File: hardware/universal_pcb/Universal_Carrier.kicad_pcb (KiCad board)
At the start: 2 copper layers, 100 x 85 mm, 24 parts, among them J1 ESP32_T_LANDSCAPE, J10 RACK_CREMALHEIRA, J11 PWR_ESP_5V, J12 PWR_SERVO_5V, J2 ESP32_B_LANDSCAPE, J3 SX1278_LORA_2x4, J4 BATT_APM, J5 BUZZER, J6 GPS_LC29H_7PIN, J7 ESC_PROP_UP, J8 RUDDER_DN, J9 WINCH_MODE, SW1 UP, SW2 MODE, SW3 DOWN, SW4 BOOT

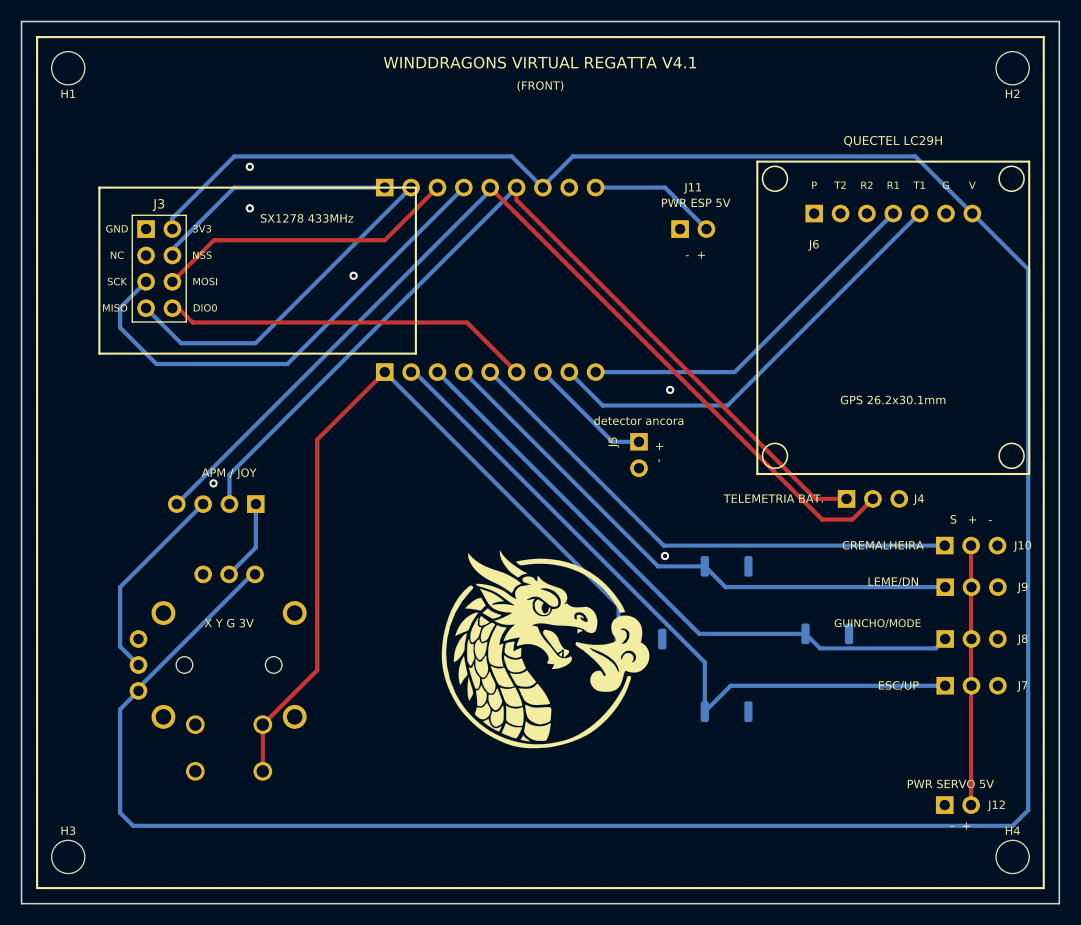
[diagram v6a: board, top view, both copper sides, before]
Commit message: feat: add ESP32-C6-LCD-1.47 hardware models and update Universal Carrier PCB design
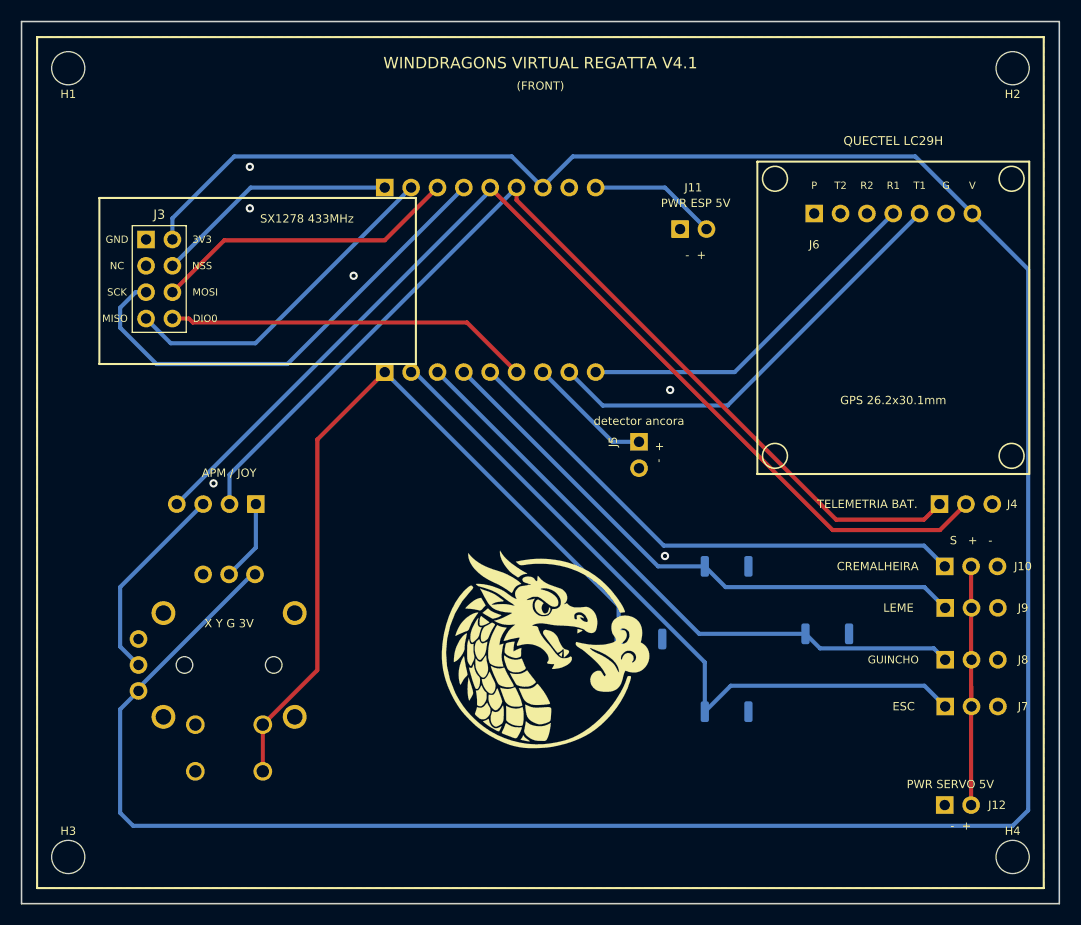
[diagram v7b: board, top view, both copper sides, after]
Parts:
- moved J4 8.97 mm to (88.5, 46.5)
- moved J10 2.00 mm to (89.0, 52.5)
- moved J7 2.00 mm to (89.0, 66.0)
- moved J8 2.00 mm to (89.0, 61.5)
- moved J9 2.00 mm to (89.0, 56.5)
- moved J3 1.00 mm to (12.0, 21.0)
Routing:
- net /IO0_ADC: track 86.9 -> 97.3 mm
- net /IO1_ADC: track 94.0 -> 103.6 mm
- net /+3V3: track 261.7 -> 263.3 mm
- net /IO12_LORA_DIO0: track 36.5 -> 35.3 mm
- net /IO4_MISO: track 33.7 -> 32.7 mm
- net /IO2_SCK: track 47.6 -> 46.7 mm
- net /IO20_RUDDER_DN: track 55.0 -> 55.8 mm
- net /IO23_ACT4: track 50.7 -> 51.6 mm
- net /IO18_ACT1_UP: track 68.8 -> 69.7 mm
- net /IO5_NSS: track 22.9 -> 23.6 mm
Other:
- board text added: "ESC"
- board text added: "GUINCHO"
- board text added: "LEME"
- board text removed: "ESC/UP"
- board text removed: "GUINCHO/MODE"
- board text removed: "LEME/DN"

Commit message: feat: update Universal Carrier PCB design and hardware configurations for I2C support
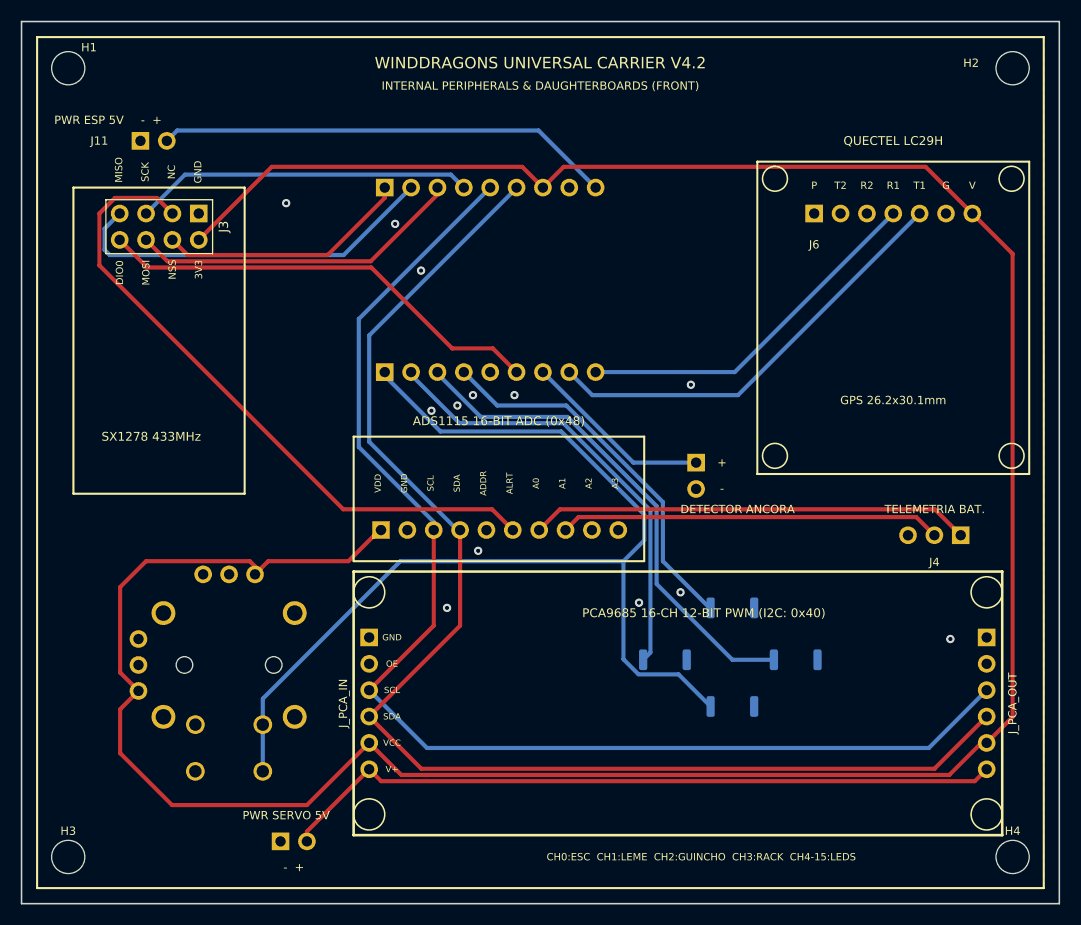
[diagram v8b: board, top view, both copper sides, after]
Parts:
- removed J10: RACK_CREMALHEIRA, Connector_PinHeader_2.54mm:PinHeader_1x03_P2.54mm_Horizontal
- removed J7: ESC_PROP_UP, Connector_PinHeader_2.54mm:PinHeader_1x03_P2.54mm_Horizontal
- removed J8: RUDDER_DN, Connector_PinHeader_2.54mm:PinHeader_1x03_P2.54mm_Horizontal
- removed J9: WINCH_MODE, Connector_PinHeader_2.54mm:PinHeader_1x03_P2.54mm_Horizontal
- removed JP_RBL: REMOVE_BEFORE_LAUNCH, Connector_PinHeader_2.54mm:PinHeader_1x04_P2.54mm_Vertical
- removed LOGO1 (x2): WindDragons_Logo, WindDragons:WindDragons_Logo_20mm
- added J_ADS: ADS1115_ADC, Connector_PinHeader_2.54mm:PinHeader_1x10_P2.54mm_Horizontal, F.Cu at (34.6, 49.0)
- added J_PCA_IN: PCA9685_IN, Connector_PinHeader_2.54mm:PinHeader_1x06_P2.54mm_Vertical, F.Cu at (33.5, 65.7)
- added J_PCA_OUT: PCA9685_OUT, Connector_PinHeader_2.54mm:PinHeader_1x06_P2.54mm_Vertical, F.Cu at (93.0, 65.7)
- J5: value BUZZER -> DETECTOR_ANCORA
- SW1: value UP -> subir ancora
- SW3: value DOWN -> largar ancora
- moved J12 64.1 mm to (25.0, 79.0)
- moved J11 52.7 mm to (11.5, 11.5)
- moved SW4 11.0 mm to (68.5, 66.0)
- moved SW1 7.76 mm to (62.0, 61.5)
- moved J5 5.85 mm to (65.0, 42.5)
- moved J3 5.66 mm to (17.1, 18.5), turned to -90 degrees
- moved SW3 4.04 mm to (68.5, 56.5)
- moved SW2 3.94 mm to (74.6, 61.5)
- moved J4 3.63 mm to (90.5, 49.5), turned to 180 degrees
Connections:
- net /IO13_BUZ renamed /IO13_ANCORA_DET
- net /IO18_ACT1_UP renamed /IO18_UP
- net /IO19_WINCH_MODE renamed /IO19_MODE
- net /IO20_RUDDER_DN renamed /IO20_DN
- J1 pad 5: /IO1_ADC -> /I2C_SCL
- J1 pad 6: /IO0_ADC -> /I2C_SDA
- J2 pad 5: /IO23_ACT4 -> /IO23_SPARE
- J4 pad 1: /IO0_ADC -> /BATT_VOLT_APM
- J4 pad 2: /IO1_ADC -> /BATT_CURR_APM
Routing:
- net /I2C_SDA: track 0.00 -> 127.9 mm
- net /I2C_SCL: track 0.00 -> 123.4 mm
- net /IO1_ADC: track 103.6 -> 0.00 mm
- net /IO0_ADC: track 97.3 -> 0.00 mm
- net /NC: track 0.00 -> 63.7 mm
- net /IO23_ACT4: track 51.6 -> 0.00 mm
- net /+5V_SERVO: track 25.0 -> 69.9 mm
- net /BATT_VOLT_APM: track 0.00 -> 42.5 mm
- net /BATT_CURR_APM: track 0.00 -> 36.8 mm
- net /+5V: track 12.3 -> 44.0 mm
- net /IO18_UP: track 69.7 -> 43.4 mm
- net /IO9_BOOT: track 78.4 -> 103.7 mm
- net /JOY_Y: track 19.5 -> 0.00 mm
- net /IO20_DN: track 55.8 -> 36.4 mm
- net /IO2_SCK: track 46.7 -> 32.7 mm
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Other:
- board text added: "+"
- board text added: "-"
- board text added: "ADS1115 16-BIT ADC (0x48)"
- board text added: "CH0:ESC CH1:LEME CH2:GUINCHO CH3:RACK CH4-15:LEDS"
- board text added: "DETECTOR ANCORA"
- board text added: "INTERNAL PERIPHERALS & DAUGHTERBOARDS (FRONT)"
- board text added: "PCA9685 16-CH 12-BIT PWM (I2C: 0x40)"
- board text added: "WINDDRAGONS REMOTE CONTROL & CARRIER V4.2"
- board text added: "WINDDRAGONS UNIVERSAL CARRIER V4.2"
- board text removed: "(FRONT)"
- board text removed: "+ -"
- board text removed: "APM / JOY"
- board text removed: "CREMALHEIRA"
- board text removed: "ESC"
- board text removed: "GUINCHO"
- board text removed: "LEME"
- board text removed: "S + -"
- board text removed: "WINDDRAGONS VIRTUAL REGATTA V4.1"
- board text removed: "X Y G 3V"
- board text removed: "detector ancora"
